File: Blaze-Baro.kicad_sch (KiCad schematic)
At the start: 0 parts

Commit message: Started blaze barometer
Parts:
- added C1: 100nF, Capacitor_SMD:C_0805_2012Metric, symbol Device:C
- added R1, R2: 10K, Resistor_SMD:R_0201_0603Metric, symbol Device:R_US
- added U1: QTStemma_F, symbol Avionics_Symbols:QTStemma_F
- added U2: MS5611, Avionics_Feet:XDCR_MS561101BA03-50, symbol Avionics_Symbols:MS5611
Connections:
- new net +3.3V: C1.1, C1.2, R1.1, R2.1, U1.1 (GND), U1.2 (V+), U2.1 (VDD), U2.2 (PS), U2.3 (GND), U2.4 (CSB), U2.5 (CSB)
- new net SCL: R2.2, U1.4 (SCL), U2.8 (SCLK)
- new net SDA: R1.2, U1.3 (SDA), U2.7 (SDA/SDI)
- no-connect marks 0 -> 1

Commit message: all past changes to blaze baro
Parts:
- removed U1: QTStemma_F, symbol Avionics_Symbols:QTStemma_F
- added U1: QTStemma_M, symbol Avionics_Symbols:QTStemma_M
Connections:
- net +3.3V: now also U1.1 (GND), U1.2 (V+)
- net SCL: now also U1.4 (SCL)
- net SDA: now also U1.3 (SDA)
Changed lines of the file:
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@@
+	)
+	(symbol
+		(lib_id "Avionics_Symbols:QTStemma_M")
+		(at 67.31 48.26 0)
+		(unit 1)
+		(exclude_from_sim no)
+		(in_bom yes)
+		(on_board yes)
+		(dnp no)
+		(fields_autoplaced yes)
+		(property "Reference" "U1"
+			(at 67.31 39.37 0)
+			(effects
+				(font
+					(size 1.27 1.27)
+				)
+			)
+		)
+		(property "Value" "QTStemma_M"
+			(at 67.31 41.91 0)
+			(effects
+				(font
+					(size 1.27 1.27)
+				)
+			)
+		)
+		(property "Footprint" ""
+			(at 67.31 48.26 0)
+			(effects
+				(font
+					(size 1.27 1.27)
+				)
+				(hide yes)
+			)
+		)
+		(property "Datasheet" ""
+			(at 67.31 48.26 0)
+			(effects
+				(font
+					(size 1.27 1.27)
+				)
+				(hide yes)
+			)
+		)
+		(property "Description" ""
+			(at 67.31 48.26 0)
+			(effects
+				(font
+					(size 1.27 1.27)
+				)
+				(hide yes)
+			)
+		)
+		(pin "2"
+		)
+		(pin "3"
+		)
+		(pin "4"
+		)
+		(pin "1"
+		)
+		(instances
+			(project ""
+				(path "/aa6f23c6-dd89-41f2-87f4-4cf630e41274"
+					(reference "U1")
+					(unit 1)
+				)
+			)
+		)
 	)
 	(symbol
@@
 					(unit 1)
 				)
-			)
-		)
-	)
-	(symbol
-		(lib_id "Avionics_Symbols:QTStemma_F")
-		(at 67.31 48.26 0)
-		(unit 1)
-		(exclude_from_sim no)
-		(in_bom yes)
-		(on_board yes)
-		(dnp no)
-		(fields_autoplaced yes)
-		(property "Reference" "U1"
-			(at 67.31 39.37 0)
-			(effects
-				(font
-					(size 1.27 1.27)
-				)
-			)
-		)
-		(property "Value" "QTStemma_F"
-			(at 67.31 41.91 0)
-			(effects
-				(font
-					(size 1.27 1.27)
-				)
-			)
-		)
-		(property "Footprint" ""
-			(at 67.31 48.26 0)
-			(effects
-				(font
-					(size 1.27 1.27)
-				)
-				(hide yes)
-			)
-		)
-		(property "Datasheet" ""
-			(at 67.31 48.26 0)
-			(effects
-				(font
-					(size 1.27 1.27)
-				)
-				(hide yes)
-			)
-		)
-		(property "Description" ""
-			(at 67.31 48.26 0)
-			(effects
-				(font
-					(size 1.27 1.27)
-				)
-				(hide yes)
-			)
-		)
-		(pin "2"
-		)
-		(pin "3"
-		)
-		(pin "4"
-		)
-		(pin "1"
-		)
-		(instances
-			(project ""
-				(path "/aa6f23c6-dd89-41f2-87f4-4cf630e41274"
-					(reference "U1")
-					(unit 1)
-				)

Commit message: push recent changes added stemma qt footprint
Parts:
- removed R1, R2: 10K, Resistor_SMD:R_0201_0603Metric, symbol Device:R_US
- added J1: Conn_01x07, symbol Connector_Generic:Conn_01x07
- C1: value 100nF -> C; footprint Capacitor_SMD:C_0805_2012Metric -> (none)
- U1: footprint (none) -> Connector_JST:JST_SH_SM02B-SRSS-TB_1x02-1MP_P1.00mm_Horizontal
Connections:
- net +3.3V: now also J1.1 (Pin_1); no longer C1.1, U1.1 (GND), U2.2 (PS), U2.3 (GND), U2.4 (CSB), U2.5 (CSB)
- net SCL: now also J1.3 (Pin_3); no longer U2.8 (SCLK)
- net SDA: now also J1.4 (Pin_4); no longer U2.7 (SDA/SDI)
- new net: U2.4 (CSB), U2.5 (CSB)
- new net GND: J1.2 (Pin_2), J1.5 (Pin_5), U1.1 (GND), U2.3 (GND)
- new net PS: J1.7 (Pin_7)
- new net SDO: J1.6 (Pin_6)
- no-connect marks 1 -> 0
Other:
- moved on the sheet: U1, U2

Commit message: Redid schematic
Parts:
- added D1: LED, symbol Device:LED
- added R1, R2, R3, R4: 1K, symbol Device:R_US
- C1: value C -> 1uF
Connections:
- net +3.3V: now also R3.2, R4.2; no longer C1.2, J1.1 (Pin_1), U1.2 (V+), U2.1 (VDD)
- net GND: now also C1.1, D1.1 (K), R2.2; no longer J1.5 (Pin_5)
- net PS: now also C1.2, J1.1 (Pin_1), U1.2 (V+), U2.1 (VDD), U2.2 (PS), R1.1
- net SCL: now also U2.8 (SCLK), R3.1
- net SDA: now also U2.7 (SDA/SDI), R4.1
- net SDO: now also U2.6 (SDO)
- net CSB: now reaches U2.4 (CSB), U2.5 (CSB)
- net CSB: now also J1.5 (Pin_5), R2.1
- new net: D1.2 (A), R1.2
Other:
- moved on the sheet: J1, U1, U2

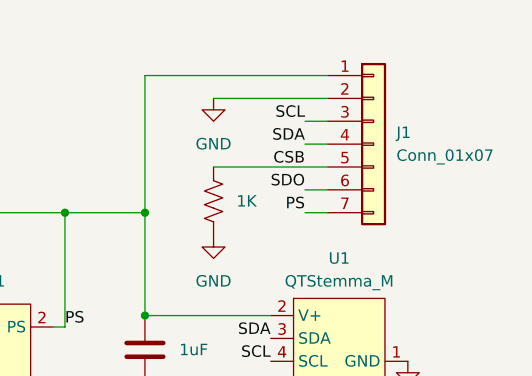
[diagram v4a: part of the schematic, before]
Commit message: Started work on pcb connections
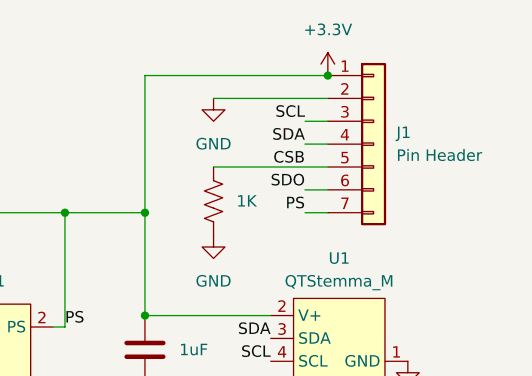
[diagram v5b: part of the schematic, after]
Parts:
- C1: footprint (none) -> Capacitor_SMD:C_0603_1608Metric
- D1: footprint (none) -> LED_SMD:LED_0603_1608Metric
- J1: value Conn_01x07 -> Pin Header; footprint (none) -> Avionics_Feet:MS5611
- R1, R2, R3, R4: footprint (none) -> Resistor_SMD:R_0603_1608Metric
- U1: footprint Connector_JST:JST_SH_SM02B-SRSS-TB_1x02-1MP_P1.00mm_Horizontal -> Connector_JST:JST_SH_SM04B-SRSS-TB_1x04-1MP_P1.00mm_Horizontal
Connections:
- net PS is gone; now on net +3.3V: C1.2, J1.1 (Pin_1), J1.7 (Pin_7), R1.1, U1.2 (V+), U2.1 (VDD), U2.2 (PS)
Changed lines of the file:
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@@
+	)
+	(junction
+		(at 134.62 33.02)
+		(diameter 0)
+		(color 0 0 0 0)
 	)
 	(junction
@@
 	(wire
 		(pts
+			(xy 132.08 40.64) (xy 134.62 40.64)
+		)
+		(stroke
+			(width 0)
+			(type default)
+		)
+	)
+	(wire
+		(pts
+			(xy 114.3 48.26) (xy 114.3 59.69)
+		)
+		(stroke
+			(width 0)
+			(type default)
+		)
+	)
+	(wire
+		(pts
+			(xy 105.41 48.26) (xy 105.41 60.96)
+		)
+		(stroke
+			(width 0)
+			(type default)
+		)
+	)
+	(wire
+		(pts
+			(xy 86.36 48.26) (xy 105.41 48.26)
+		)
+		(stroke
+			(width 0)
+			(type default)
+		)
+	)
+	(wire
+		(pts
+			(xy 72.39 48.26) (xy 74.93 48.26)
+		)
+		(stroke
+			(width 0)
+			(type default)
+		)
+	)
+	(wire
+		(pts
+			(xy 132.08 38.1) (xy 134.62 38.1)
+		)
+		(stroke
+			(width 0)
+			(type default)
+		)
+	)
+	(wire
+		(pts
+			(xy 86.36 48.26) (xy 86.36 60.96)
+		)
+		(stroke
+			(width 0)
+			(type default)
+		)
+	)
+	(wire
+		(pts
+			(xy 104.14 60.96) (xy 105.41 60.96)
+		)
+		(stroke
+			(width 0)
+			(type default)
+		)
+	)
+	(wire
+		(pts
+			(xy 121.92 43.18) (xy 134.62 43.18)
+		)
+		(stroke
+			(width 0)
+			(type default)
+		)
+	)
+	(wire
+		(pts
+			(xy 121.92 35.56) (xy 134.62 35.56)
+		)
+		(stroke
+			(width 0)
+			(type default)
+		)
+	)
+	(wire
+		(pts
+			(xy 114.3 33.02) (xy 114.3 48.26)
+		)
+		(stroke
+			(width 0)
+			(type default)
+		)
+	)
+	(wire
+		(pts
+			(xy 128.27 59.69) (xy 114.3 59.69)
+		)
+		(stroke
+			(width 0)
+			(type default)
+		)
+	)
+	(wire
+		(pts
+			(xy 82.55 48.26) (xy 86.36 48.26)
+		)
+		(stroke
+			(width 0)
+			(type default)
+		)
+	)
+	(wire
+		(pts
 			(xy 134.62 33.02) (xy 114.3 33.02)
-		)
-		(stroke
-			(width 0)
-			(type default)
-		)
-	)
-	(wire
-		(pts
-			(xy 132.08 40.64) (xy 134.62 40.64)
-		)
-		(stroke
-			(width 0)
-			(type default)
-		)
-	)
-	(wire
-		(pts
-			(xy 114.3 48.26) (xy 114.3 59.69)
-		)
-		(stroke
-			(width 0)
-			(type default)
-		)
-	)
-	(wire
-		(pts
-			(xy 105.41 48.26) (xy 105.41 60.96)
-		)
-		(stroke
-			(width 0)
-			(type default)
-		)
-	)
-	(wire
-		(pts
-			(xy 86.36 48.26) (xy 105.41 48.26)
-		)
-		(stroke
-			(width 0)
-			(type default)
-		)
-	)
-	(wire
-		(pts
-			(xy 72.39 48.26) (xy 74.93 48.26)
-		)
-		(stroke
-			(width 0)
-			(type default)
-		)
-	)
-	(wire
-		(pts
-			(xy 132.08 38.1) (xy 134.62 38.1)
-		)
-		(stroke
-			(width 0)
-			(type default)
-		)
-	)
-	(wire
-		(pts
-			(xy 86.36 48.26) (xy 86.36 60.96)
-		)
-		(stroke
-			(width 0)
-			(type default)
-		)
-	)
-	(wire
-		(pts
-			(xy 104.14 60.96) (xy 105.41 60.96)
-		)
-		(stroke
-			(width 0)
-			(type default)
-		)
-	)
-	(wire
-		(pts
-			(xy 121.92 43.18) (xy 134.62 43.18)
-		)
-		(stroke
-			(width 0)
-			(type default)
-		)
-	)
-	(wire
-		(pts
-			(xy 121.92 35.56) (xy 134.62 35.56)
-		)
-		(stroke
-			(width 0)
-			(type default)
-		)
-	)
-	(wire
-		(pts
-			(xy 114.3 33.02) (xy 114.3 48.26)
-		)
-		(stroke
-			(width 0)
-			(type default)
-		)
-	)
-	(wire
-		(pts
-			(xy 128.27 59.69) (xy 114.3 59.69)
-		)
-		(stroke
-			(width 0)
-			(type default)
-		)
-	)
-	(wire
-		(pts
-			(xy 82.55 48.26) (xy 86.36 48.26)
 		)
 		(stroke
@@
 			)
 		)
-		(property "Footprint" "Connector_JST:JST_SH_SM02B-SRSS-TB_1x02-1MP_P1.00mm_Horizontal"
+		(property "Footprint" "Connector_JST:JST_SH_SM04B-SRSS-TB_1x04-1MP_P1.00mm_Horizontal"
 			(at 135.89 62.23 0)
 			(effects
@@
 			)
 		)
-		(property "Footprint" ""
+		(property "Footprint" "Resistor_SMD:R_0603_1608Metric"
 			(at 78.486 49.276 90)
 			(effects
@@
 			)
 		)
-		(property "Footprint" ""
+		(property "Footprint" "Resistor_SMD:R_0603_1608Metric"
 			(at 133.096 86.106 90)
 			(effects
@@
 			)
 		)
-		(property "Footprint" ""
+		(property "Footprint" "LED_SMD:LED_0603_1608Metric"
 			(at 72.39 52.07 0)
 			(effects
@@
 			)
 		)
-		(property "Value" "Conn_01x07"
+		(property "Value" "Pin Header"
 			(at 142.24 41.9099 0)
 			(effects
@@
 			)
 		)
-		(property "Footprint" ""
+		(property "Footprint" "Avionics_Feet:MS5611"
 			(at 139.7 40.64 0)
 			(effects
@@
 			)
 		)
-		(property "Footprint" ""
+		(property "Footprint" "Resistor_SMD:R_0603_1608Metric"
 			(at 133.096 78.486 90)
 			(effects
@@
 			)
 		)
-		(property "Footprint" ""
+		(property "Footprint" "Capacitor_SMD:C_0603_1608Metric"
 			(at 113.3348 59.69 0)
 			(effects
@@
 	)
 	(symbol
+		(lib_id "power:+3.3V")
+		(at 134.62 33.02 0)
+		(unit 1)
+		(exclude_from_sim no)
+		(in_bom yes)
+		(on_board yes)
+		(dnp no)
+		(fields_autoplaced yes)
+		(property "Reference" "#PWR05"
+			(at 134.62 36.83 0)
+			(effects
+				(font
+					(size 1.27 1.27)
+				)
+				(hide yes)
+			)
+		)
+		(property "Value" "+3.3V"
+			(at 134.62 27.94 0)
+			(effects
+				(font
+					(size 1.27 1.27)
+				)
+			)
+		)
+		(property "Footprint" ""
+			(at 134.62 33.02 0)
+			(effects
+				(font
+					(size 1.27 1.27)
+				)
+				(hide yes)
+			)
+		)
+		(property "Datasheet" ""
+			(at 134.62 33.02 0)
+			(effects
+				(font
+					(size 1.27 1.27)
+				)
+				(hide yes)
+			)
+		)
+		(property "Description" "Power symbol creates a global label with name \"+3.3V\""
+			(at 134.62 33.02 0)
+			(effects
+				(font
+					(size 1.27 1.27)
+				)
+				(hide yes)
+			)
+		)
+		(pin "1"
+		)
+		(instances
+			(project "Blaze-Baro"
+				(path "/aa6f23c6-dd89-41f2-87f4-4cf630e41274"
+					(reference "#PWR05")
+					(unit 1)
+				)
+			)
+		)
+	)
+	(symbol
 		(lib_id "power:GND")
 		(at 104.14 73.66 0)
@@
 			)
 		)
-		(property "Footprint" ""
+		(property "Footprint" "Resistor_SMD:R_0603_1608Metric"
 			(at 122.936 47.244 90)
 			(effects

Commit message: Closer to final PCB design
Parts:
- added R5: 4.7K, Resistor_SMD:R_0603_1608Metric, symbol Device:R_US
- C1: value 1uF -> 0.1uF
- R3, R4: value 1K -> 4.7K
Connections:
- net +3.3V: now also R5.1; no longer J1.7 (Pin_7), U2.2 (PS)
- new net PS: J1.7 (Pin_7), R5.2, U2.2 (PS)
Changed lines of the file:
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@@
+	)
+	(junction
+		(at 86.36 48.26)
+		(diameter 0)
+		(color 0 0 0 0)
 	)
 	(junction
@@
 	)
 	(junction
-		(at 86.36 48.26)
-		(diameter 0)
-		(color 0 0 0 0)
-	)
-	(junction
 		(at 134.62 33.02)
 		(diameter 0)
@@
 	(wire
 		(pts
+			(xy 105.41 58.42) (xy 105.41 60.96)
+		)
+		(stroke
+			(width 0)
+			(type default)
+		)
+	)
+	(wire
+		(pts
+			(xy 86.36 48.26) (xy 105.41 48.26)
+		)
+		(stroke
+			(width 0)
+			(type default)
+		)
+	)
+	(wire
+		(pts
+			(xy 132.08 40.64) (xy 134.62 40.64)
+		)
+		(stroke
+			(width 0)
+			(type default)
+		)
+	)
+	(wire
+		(pts
+			(xy 114.3 48.26) (xy 114.3 59.69)
+		)
+		(stroke
+			(width 0)
+			(type default)
+		)
+	)
+	(wire
+		(pts
+			(xy 72.39 48.26) (xy 74.93 48.26)
+		)
+		(stroke
+			(width 0)
+			(type default)
+		)
+	)
+	(wire
+		(pts
+			(xy 132.08 38.1) (xy 134.62 38.1)
+		)
+		(stroke
+			(width 0)
+			(type default)
+		)
+	)
+	(wire
+		(pts
+			(xy 86.36 48.26) (xy 86.36 60.96)
+		)
+		(stroke
+			(width 0)
+			(type default)
+		)
+	)
+	(wire
+		(pts
+			(xy 104.14 60.96) (xy 105.41 60.96)
+		)
+		(stroke
+			(width 0)
+			(type default)
+		)
+	)
+	(wire
+		(pts
+			(xy 121.92 43.18) (xy 134.62 43.18)
+		)
+		(stroke
+			(width 0)
+			(type default)
+		)
+	)
+	(wire
+		(pts
+			(xy 121.92 35.56) (xy 134.62 35.56)
+		)
+		(stroke
+			(width 0)
+			(type default)
+		)
+	)
+	(wire
+		(pts
+			(xy 114.3 33.02) (xy 114.3 48.26)
+		)
+		(stroke
+			(width 0)
+			(type default)
+		)
+	)
+	(wire
+		(pts
+			(xy 128.27 59.69) (xy 114.3 59.69)
+		)
+		(stroke
+			(width 0)
+			(type default)
+		)
+	)
+	(wire
+		(pts
+			(xy 82.55 48.26) (xy 86.36 48.26)
+		)
+		(stroke
+			(width 0)
+			(type default)
+		)
+	)
+	(wire
+		(pts
+			(xy 134.62 33.02) (xy 114.3 33.02)
+		)
+		(stroke
+			(width 0)
+			(type default)
+		)
+	)
+	(wire
+		(pts
+			(xy 105.41 48.26) (xy 105.41 50.8)
+		)
+		(stroke
+			(width 0)
+			(type default)
+		)
+	)
+	(wire
+		(pts
+			(xy 132.08 45.72) (xy 134.62 45.72)
+		)
+		(stroke
+			(width 0)
+			(type default)
+		)
+	)
+	(wire
+		(pts
 			(xy 105.41 48.26) (xy 114.3 48.26)
-		)
-		(stroke
-			(width 0)
-			(type default)
-		)
-	)
-	(wire
-		(pts
-			(xy 132.08 40.64) (xy 134.62 40.64)
-		)
-		(stroke
-			(width 0)
-			(type default)
-		)
-	)
-	(wire
-		(pts
-			(xy 114.3 48.26) (xy 114.3 59.69)
-		)
-		(stroke
-			(width 0)
-			(type default)
-		)
-	)
-	(wire
-		(pts
-			(xy 105.41 48.26) (xy 105.41 60.96)
-		)
-		(stroke
-			(width 0)
-			(type default)
-		)
-	)
-	(wire
-		(pts
-			(xy 86.36 48.26) (xy 105.41 48.26)
-		)
-		(stroke
-			(width 0)
-			(type default)
-		)
-	)
-	(wire
-		(pts
-			(xy 72.39 48.26) (xy 74.93 48.26)
-		)
-		(stroke
-			(width 0)
-			(type default)
-		)
-	)
-	(wire
-		(pts
-			(xy 132.08 38.1) (xy 134.62 38.1)
-		)
-		(stroke
-			(width 0)
-			(type default)
-		)
-	)
-	(wire
-		(pts
-			(xy 86.36 48.26) (xy 86.36 60.96)
-		)
-		(stroke
-			(width 0)
-			(type default)
-		)
-	)
-	(wire
-		(pts
-			(xy 104.14 60.96) (xy 105.41 60.96)
-		)
-		(stroke
-			(width 0)
-			(type default)
-		)
-	)
-	(wire
-		(pts
-			(xy 121.92 43.18) (xy 134.62 43.18)
-		)
-		(stroke
-			(width 0)
-			(type default)
-		)
-	)
-	(wire
-		(pts
-			(xy 121.92 35.56) (xy 134.62 35.56)
-		)
-		(stroke
-			(width 0)
-			(type default)
-		)
-	)
-	(wire
-		(pts
-			(xy 114.3 33.02) (xy 114.3 48.26)
-		)
-		(stroke
-			(width 0)
-			(type default)
-		)
-	)
-	(wire
-		(pts
-			(xy 128.27 59.69) (xy 114.3 59.69)
-		)
-		(stroke
-			(width 0)
-			(type default)
-		)
-	)
-	(wire
-		(pts
-			(xy 82.55 48.26) (xy 86.36 48.26)
-		)
-		(stroke
-			(width 0)
-			(type default)
-		)
-	)
-	(wire
-		(pts
-			(xy 134.62 33.02) (xy 114.3 33.02)
-		)
-		(stroke
-			(width 0)
-			(type default)
-		)
-	)
-	(wire
-		(pts
-			(xy 132.08 45.72) (xy 134.62 45.72)
 		)
 		(stroke
@@
 			)
 		)
-		(property "Value" "1K"
+		(property "Value" "4.7K"
 			(at 133.35 81.28 90)
 			(effects
@@
 	(symbol
 		(lib_id "Device:R_US")
+		(at 105.41 54.61 0)
+		(unit 1)
+		(exclude_from_sim no)
+		(in_bom yes)
+		(on_board yes)
+		(dnp no)
+		(fields_autoplaced yes)
+		(property "Reference" "R5"
+			(at 99.06 54.61 90)
+			(effects
+				(font
+					(size 1.27 1.27)
+				)
+				(hide yes)
+			)
+		)
+		(property "Value" "4.7K"
+			(at 107.95 54.6099 0)
+			(effects
+				(font
+					(size 1.27 1.27)
+				)
+				(justify left)
+			)
+		)
+		(property "Footprint" "Resistor_SMD:R_0603_1608Metric"
+			(at 106.426 54.864 90)
+			(effects
+				(font
+					(size 1.27 1.27)
+				)
+				(hide yes)
+			)
+		)
+		(property "Datasheet" "~"
+			(at 105.41 54.61 0)
+			(effects
+				(font
+					(size 1.27 1.27)
+				)
+				(hide yes)
+			)
+		)
+		(property "Description" "Resistor, US symbol"
+			(at 105.41 54.61 0)
+			(effects
+				(font
+					(size 1.27 1.27)
+				)
+				(hide yes)
+			)
+		)
+		(pin "2"
+		)
+		(pin "1"
+		)
+		(instances
+			(project "Blaze-Baro"
+				(path "/aa6f23c6-dd89-41f2-87f4-4cf630e41274"
+					(reference "R5")
+					(unit 1)
+				)
+			)
+		)
+	)
+	(symbol
+		(lib_id "Device:R_US")
 		(at 133.35 77.47 270)
 		(unit 1)
@@
 			)
 		)
-		(property "Value" "1K"
+		(property "Value" "4.7K"
 			(at 133.35 73.66 90)
 			(effects
@@
 			)
 		)
-		(property "Value" "1uF"
+		(property "Value" "0.1uF"
 			(at 118.11 63.4999 0)
 			(effects
